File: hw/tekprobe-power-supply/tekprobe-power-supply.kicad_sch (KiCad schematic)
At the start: 22 parts

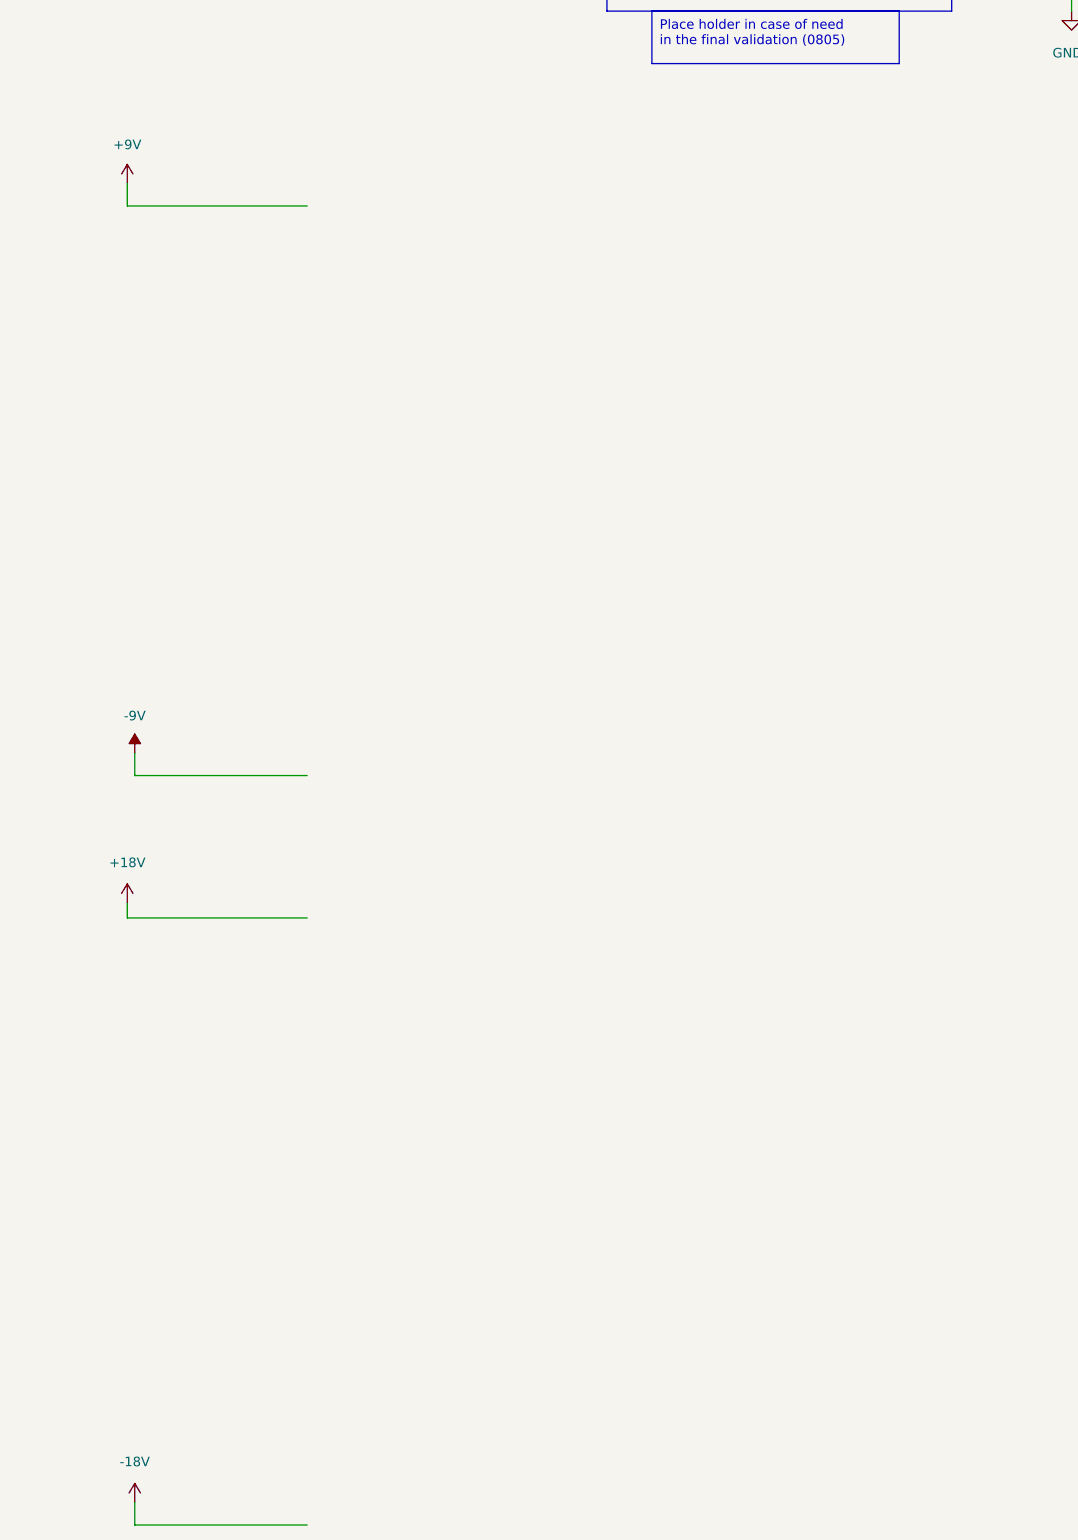
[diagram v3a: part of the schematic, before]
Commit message: añadido nuevos LDO
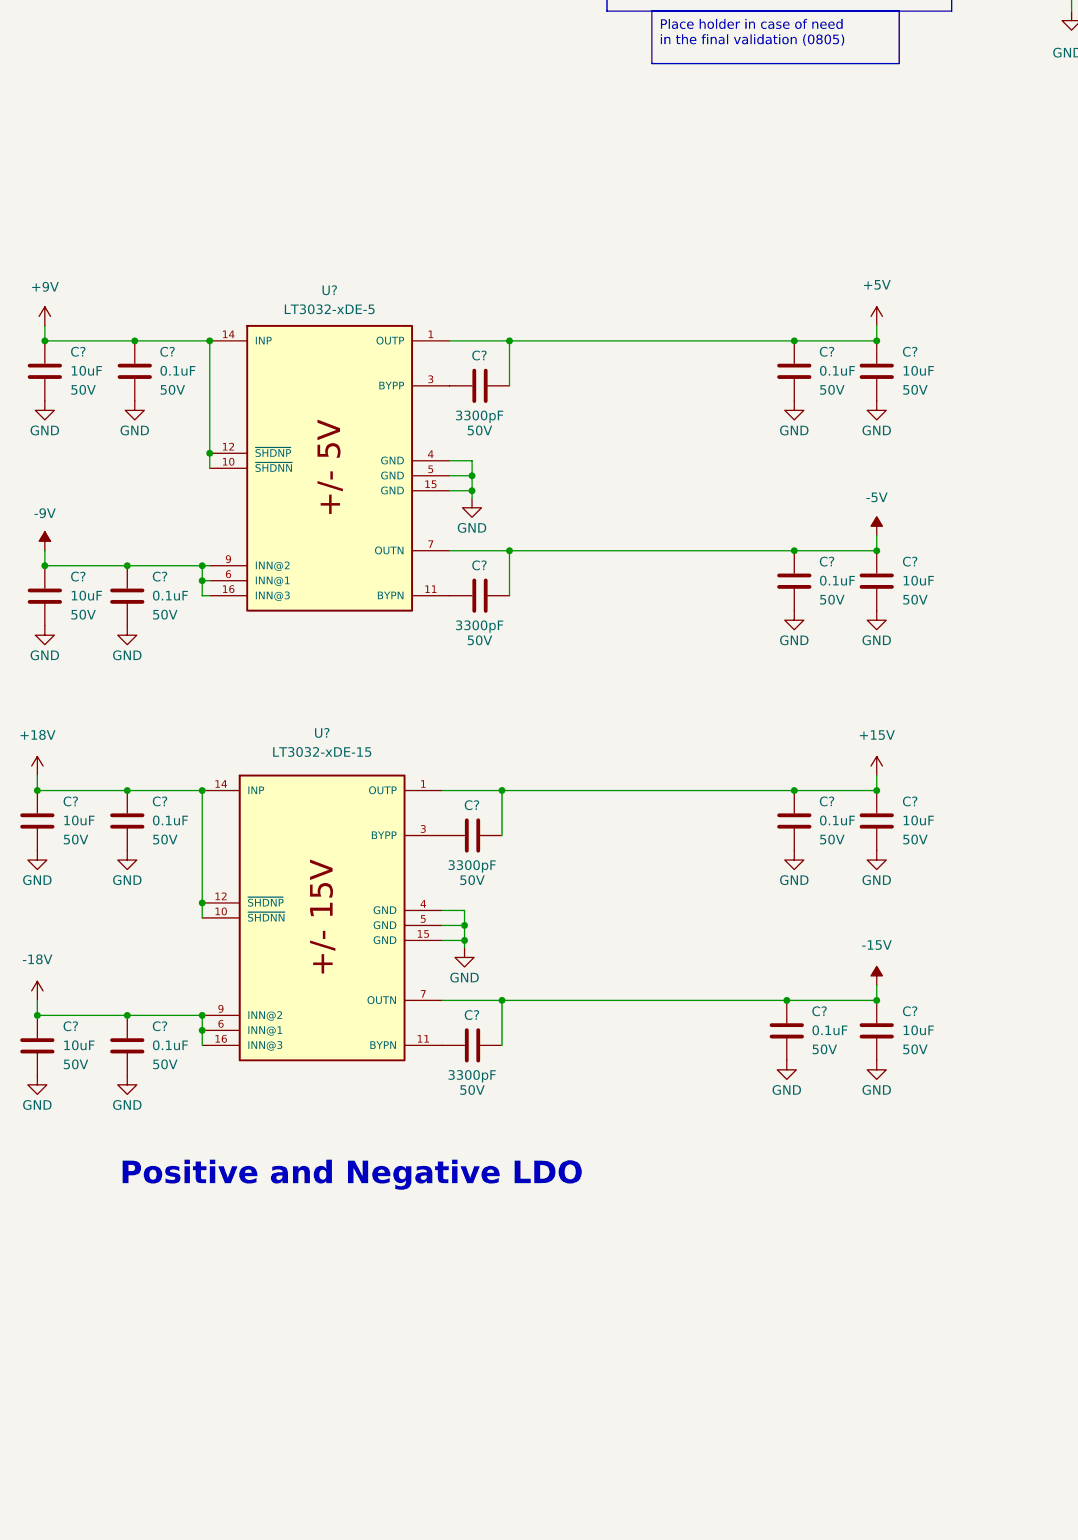
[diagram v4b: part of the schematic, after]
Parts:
- added C? (x8): 10uF, Capacitor_SMD:C_0805_2012Metric, symbol Herranz - Capacitor (0805):Gen_C
- added C? (x8): 0.1uF, Capacitor_SMD:C_0805_2012Metric, symbol Herranz - Capacitor (0805):Gen_C
- added C? (x4): 3300pF, Capacitor_SMD:C_0805_2012Metric, symbol Herranz - Capacitor (0805):Gen_C
- added U?: LT3032-xDE-15, Herranz - Linear Regulators:SON50P300X400X80-15N, symbol Herranz - Linear Regulators:LT3032-xDE-15
- added U?: LT3032-xDE-5, Herranz - Linear Regulators:SON50P300X400X80-15N, symbol Herranz - Linear Regulators:LT3032-xDE-5
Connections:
- net +7.5V: now also C?.1, C?.1, C?.1, C?.1, U?.10 (~{SHDNN}), U?.12 (~{SHDNP}), U?.14 (INP), U?.16 (INN@3), U?.6 (INN@1), U?.9 (INN@2)
- net +9V: now also C?.1, C?.1, U?.10 (~{SHDNN}), U?.12 (~{SHDNP}), U?.14 (INP)
- net -9V: now also C?.1, C?.1, U?.16 (INN@3), U?.6 (INN@1), U?.9 (INN@2)
- net GND: now also C?.2, C?.2, C?.2, C?.2, C?.2, C?.2, C?.2, C?.2, C?.2, C?.2, C?.2, C?.2, C?.2, C?.2, C?.2, C?.2, U?.15 (GND), U?.15 (GND), U?.4 (GND), U?.4 (GND), U?.5 (GND), U?.5 (GND)
- new net: C?.1, U?.11 (BYPN) (x2)
- new net: C?.1, U?.3 (BYPP) (x2)
- new net +15V: C?.1, C?.1, C?.2, U?.1 (OUTP)
- new net +5V: C?.1, C?.1, C?.2, U?.1 (OUTP)
- new net -15V: C?.1, C?.1, C?.2, U?.7 (OUTN)
- new net -5V: C?.1, C?.1, C?.2, U?.7 (OUTN)
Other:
- note added: "Positive and Negative LDO"
